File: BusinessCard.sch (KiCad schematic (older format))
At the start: 8 parts, among them Q1 Q_NMOS_DGS

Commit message: First draft of front
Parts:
- added P1, P2, P3, P4: ButtonPad, CardElements:ButtonPad, symbol ButtonPad
- BT1: footprint (none) -> CardElements:Linx_CR2032_Holder
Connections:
- net +3V3: now also P4.1
- net GND: now also P2.1
- net Sense: now also P1.1, P3.1
- net Cathode: now reaches D1.1 (K), D2.1 (K), D3.1 (K), D4.1 (K), D5.1 (K), D6.1 (K), Q1.1 (D)
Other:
- moved on the sheet: Q1
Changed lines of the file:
@@
 LIBS:contrib
 LIBS:valves
+LIBS:CardElements
 LIBS:BusinessCard-cache
 EELAYER 25 0
@@
 F 0 "BT1" H 4150 3900 50  0000 L CNN
 F 1 "Battery_Cell" H 4150 3800 50  0000 L CNN
-F 2 "" V 4050 3860 50  0001 C CNN
+F 2 "CardElements:Linx_CR2032_Holder" V 4050 3860 50  0001 C CNN
 F 3 "" V 4050 3860 50  0001 C CNN
 	1    4050 3800
@@
 L Q_NMOS_DGS Q1
 U 1 1 59ADBCA5
-P 5100 4250
-F 0 "Q1" H 5300 4300 50  0000 L CNN
-F 1 "Q_NMOS_DGS" H 5300 4200 50  0000 L CNN
-F 2 "TO_SOT_Packages_SMD:SOT-23_Handsoldering" H 5300 4350 50  0001 C CNN
-F 3 "" H 5100 4250 50  0001 C CNN
-	1    5100 4250
-	1    0    0    -1
+P 5300 4300
+F 0 "Q1" H 5500 4350 50  0000 L CNN
+F 1 "Q_NMOS_DGS" H 5500 4250 50  0000 L CNN
+F 2 "TO_SOT_Packages_SMD:SOT-23_Handsoldering" H 5500 4400 50  0001 C CNN
+F 3 "" H 5300 4300 50  0001 C CNN
+	1    5300 4300
+	-1   0    0    -1
 $EndComp
 Wire Wire Line
@@
 	4800 4000 6300 4000
 Wire Wire Line
-	5200 4000 5200 4050
+	5200 4000 5200 4100
 Wire Wire Line
 	5100 3900 5100 4000
@@
 Connection ~ 5400 3450
 $Comp
-L GND #PWR2
+L GND #PWR01
 U 1 1 59ADBDD4
 P 5200 4550
-F 0 "#PWR2" H 5200 4300 50  0001 C CNN
+F 0 "#PWR01" H 5200 4300 50  0001 C CNN
 F 1 "GND" H 5200 4400 50  0000 C CNN
 F 2 "" H 5200 4550 50  0001 C CNN
@@
 $EndComp
 $Comp
-L GND #PWR1
+L GND #PWR02
 U 1 1 59ADBDFA
 P 4050 4000
-F 0 "#PWR1" H 4050 3750 50  0001 C CNN
+F 0 "#PWR02" H 4050 3750 50  0001 C CNN
 F 1 "GND" H 4050 3850 50  0000 C CNN
 F 2 "" H 4050 4000 50  0001 C CNN
@@
 	4050 3900 4050 4000
 Wire Wire Line
-	5200 4450 5200 4550
+	5200 4500 5200 4550
 $Comp
 L LED D5
@@
 	6300 4000 6300 3900
 Connection ~ 6000 4000
-Text GLabel 4800 4250 0    60   Input ~ 0
-Sense
-Wire Wire Line
-	4800 4250 4900 4250
-$Comp
-L +3.3V #PWR?
+$Comp
+L +3.3V #PWR03
 U 1 1 59BF43B7
 P 4050 3400
-F 0 "#PWR?" H 4050 3250 50  0001 C CNN
+F 0 "#PWR03" H 4050 3250 50  0001 C CNN
 F 1 "+3.3V" H 4050 3540 50  0000 C CNN
 F 2 "" H 4050 3400 50  0001 C CNN
@@
 $EndComp
 Connection ~ 4050 3450
+$Comp
+L ButtonPad P1
+U 1 1 59C81A4A
+P 5950 4500
+F 0 "P1" H 6250 4550 60  0000 L CNN
+F 1 "ButtonPad" H 6250 4450 60  0001 L CNN
+F 2 "CardElements:ButtonPad" H 5950 4500 60  0001 C CNN
+F 3 "" H 5950 4500 60  0001 C CNN
+	1    5950 4500
+	-1   0    0    -1
+$EndComp
+$Comp
+L ButtonPad P2
+U 1 1 59C81A90
+P 5950 4700
+F 0 "P2" H 6250 4750 60  0000 L CNN
+F 1 "ButtonPad" H 6250 4650 60  0001 L CNN
+F 2 "CardElements:ButtonPad" H 5950 4700 60  0001 C CNN
+F 3 "" H 5950 4700 60  0001 C CNN
+	1    5950 4700
+	-1   0    0    1
+$EndComp
+$Comp
+L ButtonPad P3
+U 1 1 59C81B3A
+P 6450 4500
+F 0 "P3" H 6750 4550 60  0000 L CNN
+F 1 "ButtonPad" H 6750 4450 60  0001 L CNN
+F 2 "CardElements:ButtonPad" H 6450 4500 60  0001 C CNN
+F 3 "" H 6450 4500 60  0001 C CNN
+	1    6450 4500
+	1    0    0    -1
+$EndComp
+$Comp
+L ButtonPad P4
+U 1 1 59C81B40
+P 6450 4700
+F 0 "P4" H 6750 4750 60  0000 L CNN
+F 1 "ButtonPad" H 6750 4650 60  0001 L CNN
+F 2 "CardElements:ButtonPad" H 6450 4700 60  0001 C CNN
+F 3 "" H 6450 4700 60  0001 C CNN
+	1    6450 4700
+	1    0    0    1
+$EndComp
+Wire Wire Line
+	5500 4300 6450 4300
+Wire Wire Line
+	5950 4300 5950 4350
+Wire Wire Line
+	6450 4300 6450 4350
+Connection ~ 5950 4300
+$Comp
+L GND #PWR04
+U 1 1 59C81C52
+P 5950 4950
+F 0 "#PWR04" H 5950 4700 50  0001 C CNN
+F 1 "GND" H 5950 4800 50  0000 C CNN
+F 2 "" H 5950 4950 50  0001 C CNN
+F 3 "" H 5950 4950 50  0001 C CNN
+	1    5950 4950
+	1    0    0    -1
+$EndComp
+Wire Wire Line
+	5950 4850 5950 4950
+$Comp
+L +3.3V #PWR05
+U 1 1 59C81EC0
+P 7100 4850
+F 0 "#PWR05" H 7100 4700 50  0001 C CNN
+F 1 "+3.3V" H 7100 4990 50  0000 C CNN
+F 2 "" H 7100 4850 50  0001 C CNN
+F 3 "" H 7100 4850 50  0001 C CNN
+	1    7100 4850
+	1    0    0    -1
+$EndComp
+Wire Wire Line
+	6450 4850 6450 4950
+Wire Wire Line
+	6450 4950 7100 4950
+Wire Wire Line
+	7100 4950 7100 4850
+Text GLabel 6450 4300 2    60   Input ~ 0
+Sense
+Text GLabel 6300 4000 2    60   Input ~ 0
+Cathode
 $EndSCHEMATC

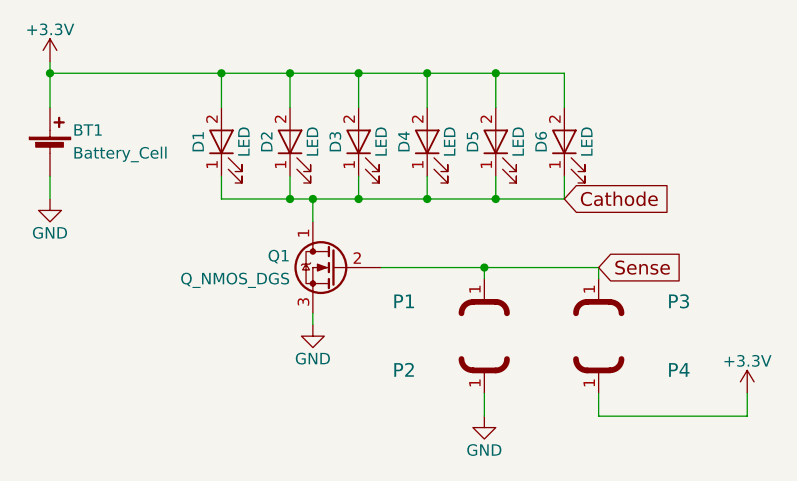
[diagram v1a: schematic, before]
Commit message: Add filtering components, back silkscreen
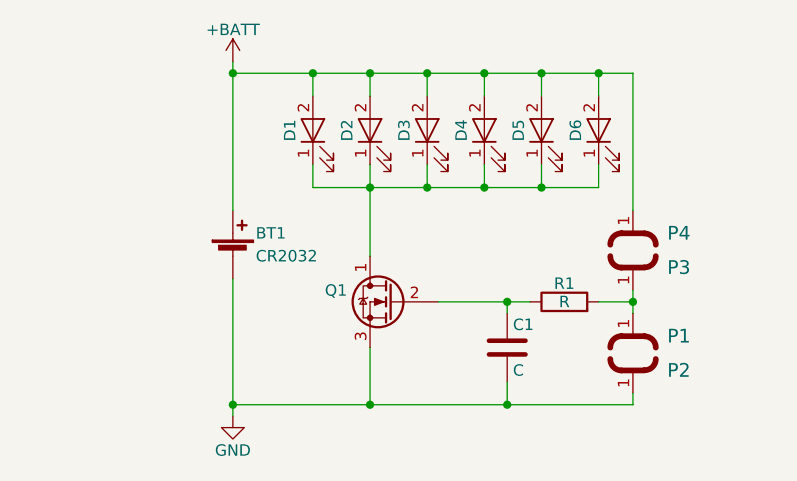
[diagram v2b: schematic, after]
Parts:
- added C1: C, Capacitors_SMD:C_1206_HandSoldering, symbol C
- added R1: R, Resistors_SMD:R_1206_HandSoldering, symbol R
- BT1: value Battery_Cell -> CR2032
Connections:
- net GND: now also C1.2
- net +3V3 renamed +BATT
- net Cathode: no longer names the net of D1.1 (K), D2.1 (K), D3.1 (K), D4.1 (K), D5.1 (K), D6.1 (K), Q1.1 (D)
- net Sense: no longer names the net of P1.1, P3.1
- net Sense: now also R1.2; no longer Q1.2 (G)
- new net: C1.1, Q1.2 (G), R1.1
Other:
- moved on the sheet: BT1, D1, D2, D3, D4, D5, D6, P1, P2, P3, P4, Q1
